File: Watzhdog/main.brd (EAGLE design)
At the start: 100 x 80 mm, 43 parts, among them CN1 MICROUSB(MC-5F-02), IC1 C8051F381-GM, IC3 N25Q512A, IC6 MPU-9250, U1 MCP73831, U2 TPS61201

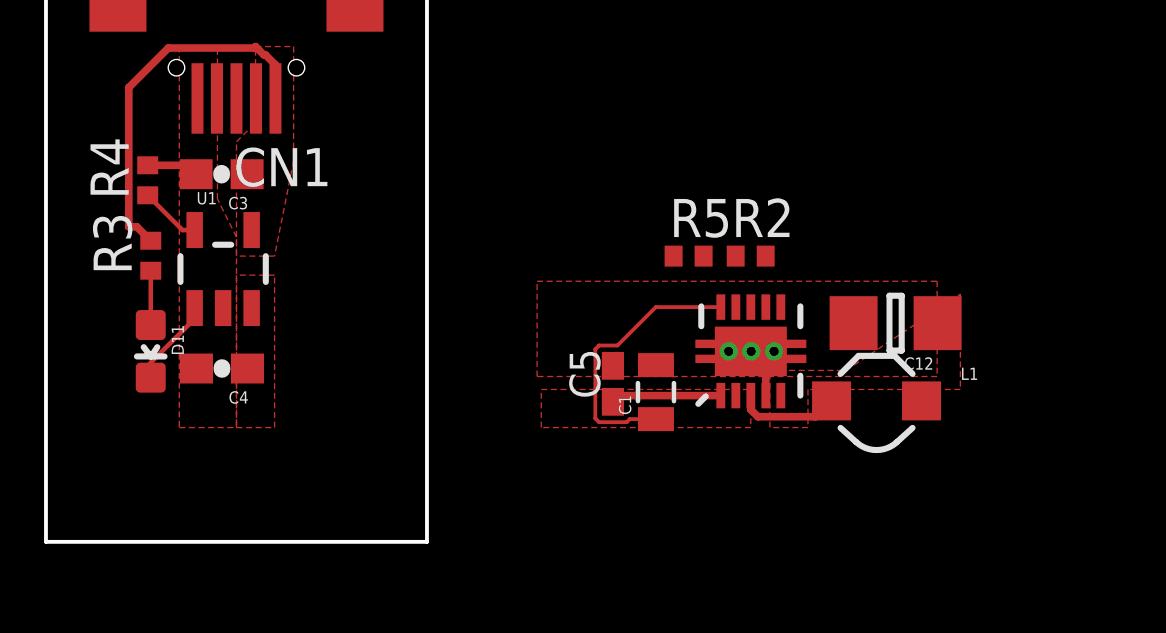
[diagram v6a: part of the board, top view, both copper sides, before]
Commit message: Modified dc-dc converter curcuit
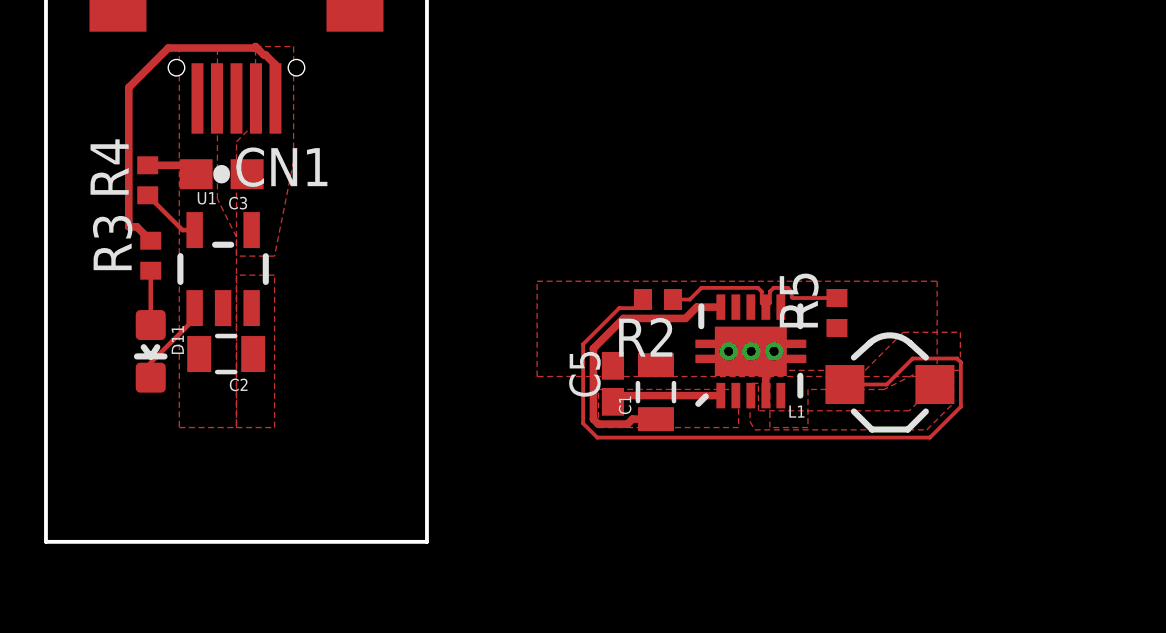
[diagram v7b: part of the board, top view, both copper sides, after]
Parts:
- removed C12: 10uF, CH_passive:1206
- removed C4: 4.7uF, SparkFun-Capacitors:0603-CAP
- added C2: 22uF, CH_passive:0805
- D2, D4: value (none) -> CUS08F30
- moved R5 5.30 mm to (77.2, 52.1), turned to 90 degrees
- moved R2 3.41 mm to (71.2, 52.5), turned to 180 degrees
- moved L1 0.70 mm to (78.9, 49.7), turned to 180 degrees
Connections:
- net DGND: now also C2.2; no longer C12.2, C4.2
- net VBAT: now also C2.1; no longer C12.1, C4.1
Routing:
- net VBAT: track 4.10 -> 28.3 mm
- net UVLO: track 0.00 -> 6.84 mm
- net N$2: track 3.48 -> 0.00 mm
- added copper zone on layer 1, net N$2

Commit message: Modified curcuit
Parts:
- moved R5 23.5 mm to (54.6, 45.4), turned to 180 degrees
- moved L1 22.1 mm to (57.0, 47.2), turned to 270 degrees
- moved R2 21.5 mm to (54.2, 39.5), turned to 270 degrees
- moved U2 20.2 mm to (55.9, 42.5), turned to 90 degrees
- moved C5 17.3 mm to (57.0, 37.9), turned to 180 degrees
- moved C1 17.2 mm to (57.2, 39.4), turned to 180 degrees
- moved JP1 8.25 mm to (57.2, 30.3)
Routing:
- net N$4: track 12.7 -> 0.00 mm
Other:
- outline, holes or cut-outs redrawn
